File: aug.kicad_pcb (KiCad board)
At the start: 2 copper layers, 25 parts, among them J1 Conn_01x22_Socket, J2 Conn_01x22_Socket, J3 24V_IN, J4 LED_WHITE, J5 LED_RED, J6 Display Connector, J7 BME280 Connector, Q1 SI2356DS-T1-BE3, Q2 SI2356DS-T1-BE3, U1 TSR1-2450E

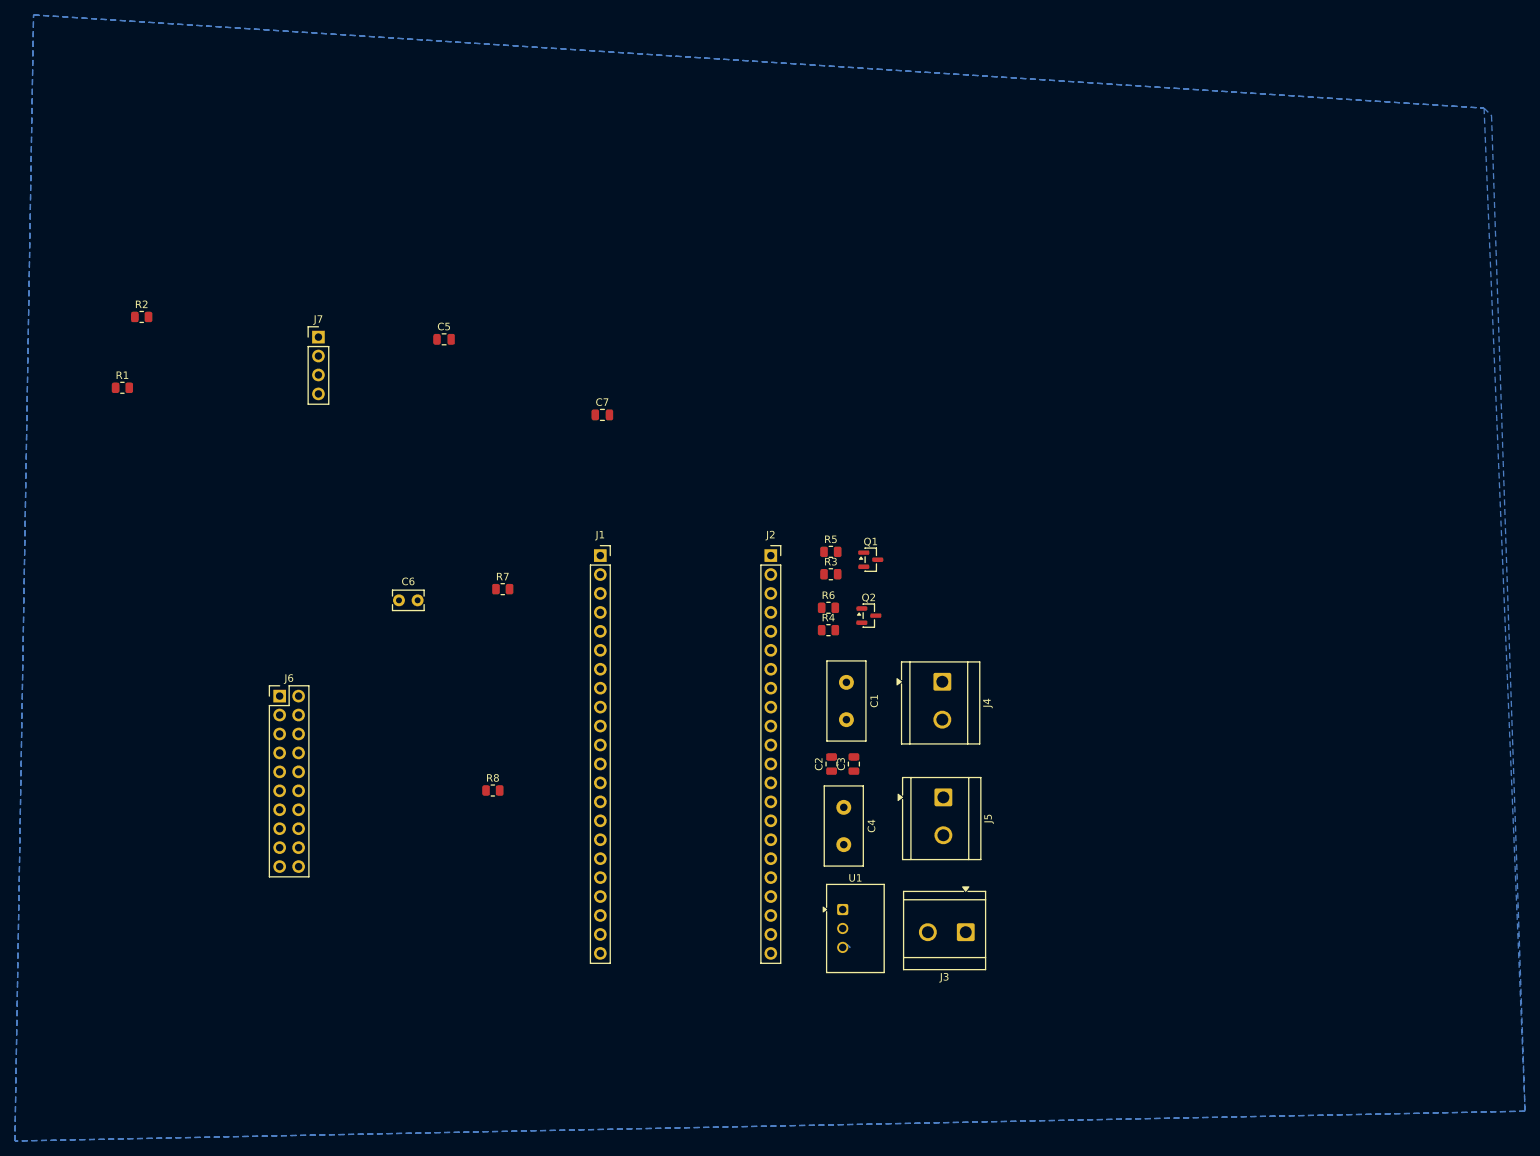
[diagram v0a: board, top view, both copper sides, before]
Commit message: PCB version 1. Ordered.
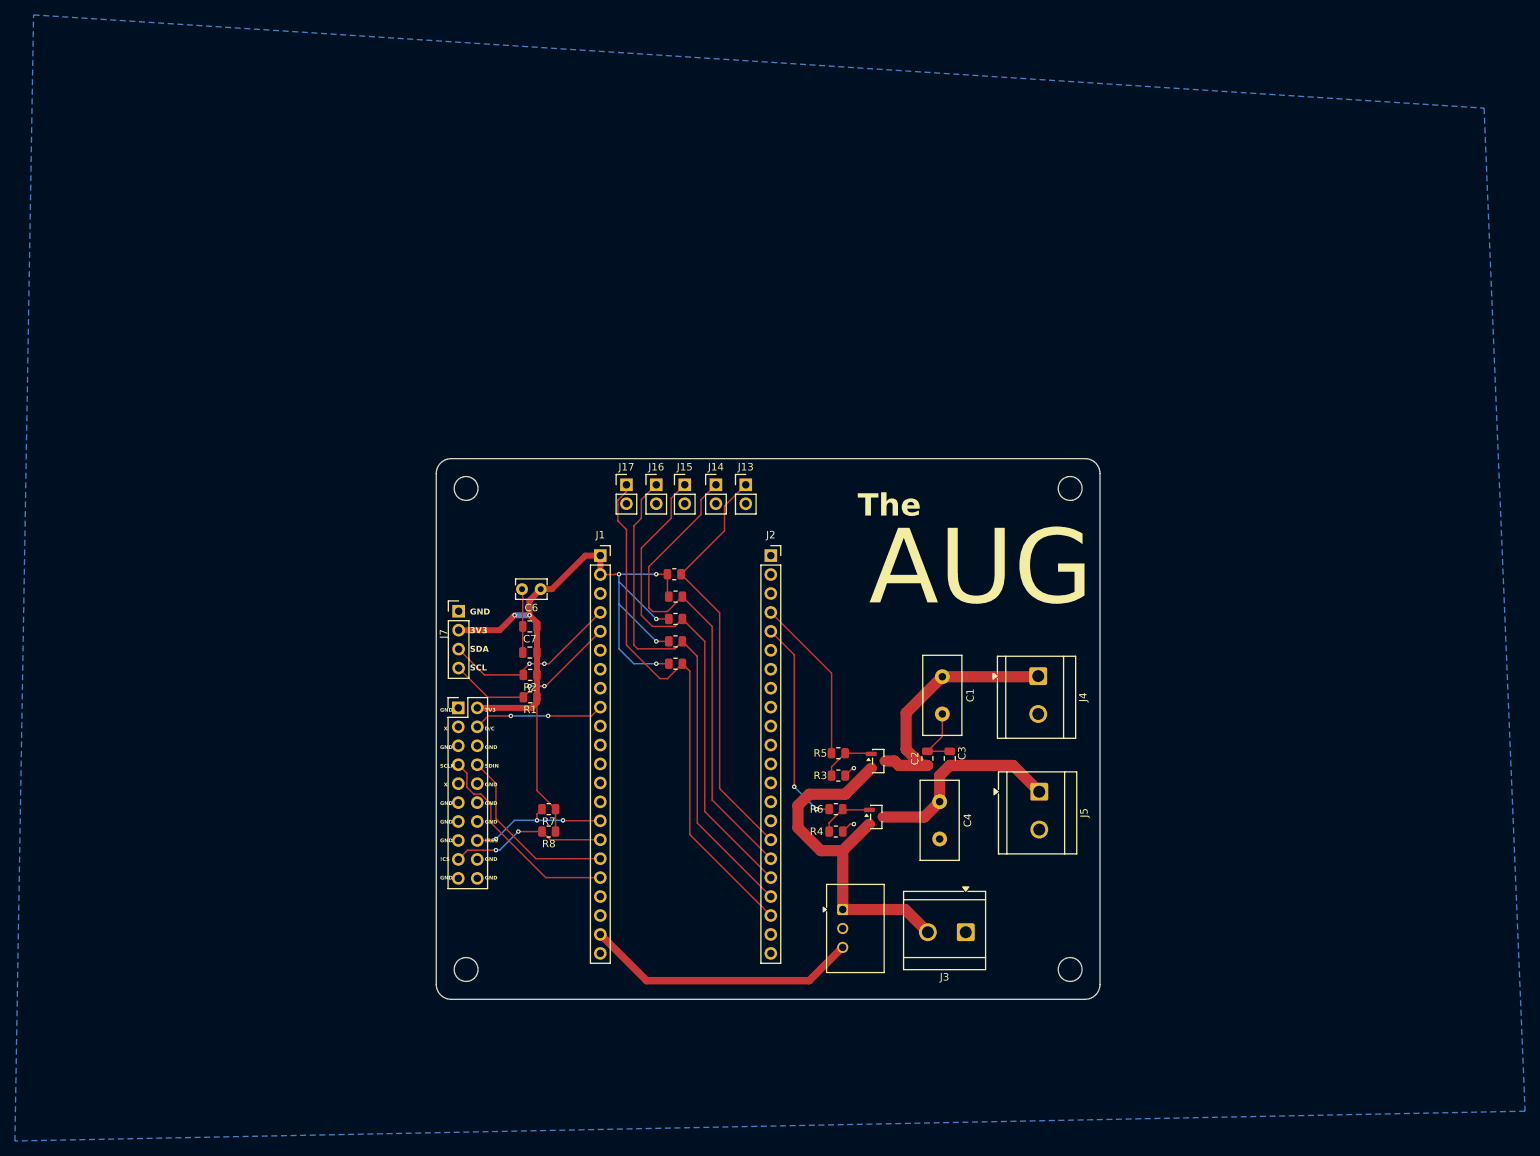
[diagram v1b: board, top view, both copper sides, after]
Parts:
- added H1: MountingHole, MountingHole:MountingHole_3.2mm_M3, F.Cu at (82.0, 91.0)
- added H2: MountingHole, MountingHole:MountingHole_3.2mm_M3, F.Cu at (163.0, 91.0)
- added H3: MountingHole, MountingHole:MountingHole_3.2mm_M3, F.Cu at (82.0, 155.5)
- added H4: MountingHole, MountingHole:MountingHole_3.2mm_M3, F.Cu at (163.0, 155.5)
- added J13: Conn_01x02, Connector_PinHeader_2.54mm:PinHeader_1x02_P2.54mm_Vertical, F.Cu at (119.5, 90.5)
- added J14: Conn_01x02, Connector_PinHeader_2.54mm:PinHeader_1x02_P2.54mm_Vertical, F.Cu at (115.5, 90.5)
- added J15: Conn_01x02, Connector_PinHeader_2.54mm:PinHeader_1x02_P2.54mm_Vertical, F.Cu at (111.3, 90.5)
- added J16: Conn_01x02, Connector_PinHeader_2.54mm:PinHeader_1x02_P2.54mm_Vertical, F.Cu at (107.5, 90.5)
- added J17: Conn_01x02, Connector_PinHeader_2.54mm:PinHeader_1x02_P2.54mm_Vertical, F.Cu at (103.5, 90.5)
- added R10: 10k, Resistor_SMD:R_0805_2012Metric, F.Cu at (110.1, 111.5)
- added R11: 10k, Resistor_SMD:R_0805_2012Metric, F.Cu at (110.1, 108.5)
- added R12: 10k, Resistor_SMD:R_0805_2012Metric, F.Cu at (110.1, 105.5)
- added R13: 10k, Resistor_SMD:R_0805_2012Metric, F.Cu at (109.9, 102.5)
- added R9: 10k, Resistor_SMD:R_0805_2012Metric, F.Cu at (110.1, 114.5)
- moved R2 70.8 mm to (90.6, 116.0), turned to 180 degrees
- moved R1 68.6 mm to (90.6, 119.0), turned to 180 degrees
- moved C5 43.5 mm to (90.5, 113.0), turned to 180 degrees
- moved J7 41.3 mm to (81.0, 107.5)
- moved R7 30.1 mm to (93.1, 134.0), turned to 180 degrees
- moved C7 30.0 mm to (90.5, 109.5), turned to 180 degrees
- moved Q2 27.0 mm to (137.0, 135.1)
- moved Q1 27.0 mm to (137.3, 127.5)
- moved R3 27.0 mm to (131.9, 129.5)
- moved R4 27.0 mm to (131.6, 137.0)
- moved R5 27.0 mm to (131.9, 126.5)
- moved R6 27.0 mm to (131.6, 134.0)
- moved J6 24.0 mm to (81.0, 120.4)
- moved C6 19.1 mm to (92.0, 104.5), turned to 180 degrees
- moved J4 12.9 mm to (158.7, 116.2)
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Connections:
- J1 pad 10: Net-(J1-GPIO17) -> unconnected-(J1-GPIO17-Pad10)
- J1 pad 11: Net-(J1-GPIO18) -> unconnected-(J1-GPIO18-Pad11)
- J1 pad 12: Net-(J1-GPIO8) -> unconnected-(J1-GPIO8-Pad12)
- J1 pad 15: unconnected-(J1-GPIO9-Pad15) -> Net-(J1-GPIO9)
- J1 pad 17: unconnected-(J1-GPIO11-Pad17) -> Net-(J1-GPIO11)
- J1 pad 18: unconnected-(J1-GPIO12-Pad18) -> Net-(J1-GPIO12)
- J2 pad 16: unconnected-(J2-GPIO48-Pad16) -> Net-(J13-Pin_1)
- J2 pad 17: unconnected-(J2-GPIO47-Pad17) -> Net-(J14-Pin_1)
- J2 pad 18: unconnected-(J2-GPIO21-Pad18) -> Net-(J15-Pin_1)
- J2 pad 19: unconnected-(J2-GPIO20-Pad19) -> Net-(J16-Pin_1)
- J2 pad 20: unconnected-(J2-GPIO19-Pad20) -> Net-(J17-Pin_1)
- J3 pad 1: Net-(J3-Pin_1) -> GND
- J3 pad 2: GND -> Net-(J3-Pin_2)
- J6 pad 16: Net-(J1-GPIO10) -> Net-(J1-GPIO9)
- J6 pad 17: Net-(J1-GPIO17) -> Net-(J1-GPIO10)
- J6 pad 7: Net-(J1-GPIO8) -> Net-(J1-GPIO12)
- J6 pad 8: Net-(J1-GPIO18) -> Net-(J1-GPIO11)
- Q1 pad 2: GND -> Net-(J3-Pin_2)
- Q2 pad 2: GND -> Net-(J3-Pin_2)
- R7 pad 2: Net-(J1-GPIO17) -> Net-(J1-GPIO9)
- R8 pad 2: Net-(J1-GPIO8) -> Net-(J1-GPIO10)
- U1 pad 1: Net-(J3-Pin_1) -> Net-(J3-Pin_2)
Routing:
- net +3V3: track 0.00 -> 114.1 mm, vias 0 -> 7
- net Net-(J17-Pin_1): track 0.00 -> 71.3 mm
- net Net-(J16-Pin_1): track 0.00 -> 69.0 mm
- net Net-(J15-Pin_1): track 0.00 -> 66.0 mm
- net Net-(J14-Pin_1): track 0.00 -> 65.8 mm
- net Net-(J13-Pin_1): track 0.00 -> 56.2 mm
- net Net-(J3-Pin_2): track 0.00 -> 48.0 mm
- net Net-(J1-5V): track 0.49 -> 36.9 mm
- net Net-(J4-Pin_1): track 0.00 -> 34.3 mm
- net Net-(J2-GPIO2): track 0.00 -> 28.1 mm, vias 0 -> 2
- net Net-(J1-GPIO12): track 0.00 -> 27.9 mm
- net Net-(J5-Pin_1): track 0.00 -> 27.3 mm
- net Net-(J1-GPIO5): track 0.23 -> 24.9 mm, vias 0 -> 2
- net Net-(J1-GPIO11): track 0.00 -> 24.5 mm
- net Net-(J1-GPIO4): track 0.00 -> 24.3 mm, vias 0 -> 2
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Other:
- board outline added: 89 x 72.5 mm
- board text added: "!CS"
- board text added: "!RES"
- board text added: "3V3"
- board text added: "AUG"
- board text added: "D/C"
- board text added: "GND"
- board text added: "SCL"
- board text added: "SCLK"
- board text added: "SDA"
- board text added: "SDIN"
- board text added: "The"
- board text added: "X"
